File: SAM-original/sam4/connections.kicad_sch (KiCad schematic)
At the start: 23 parts, among them J18 XT60PW-M, J19 XT60PW-M, J20 XT30PW-F, J21 Conn_02x16_Odd_Even, J22 10103594-0001LF, J23 Conn_01x06_Socket, J24 Conn_01x04_Socket, J25 Conn_01x04_Socket, J26 Conn_01x04_Socket, J27 Conn_01x04_Socket, J28 Conn_01x04_Socket, J5 Conn_01x09_Socket, J6 Conn_01x02_Socket, J7 Conn_01x06_Socket, J8 Conn_01x02_Socket, SW1 SW_SPST

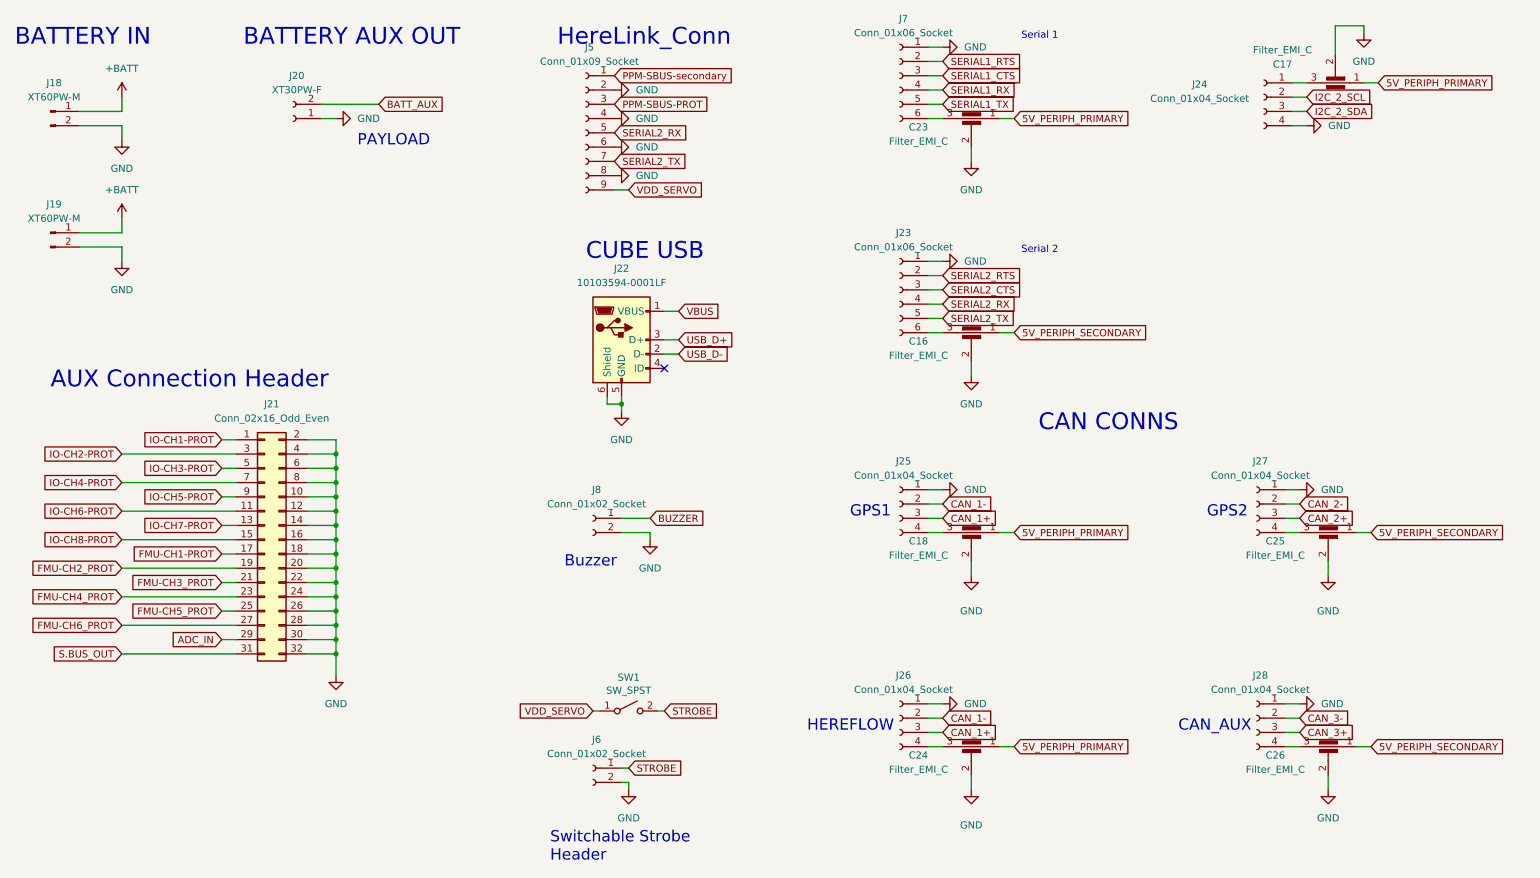
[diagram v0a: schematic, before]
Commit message: reannotate sam schem to bring into parity
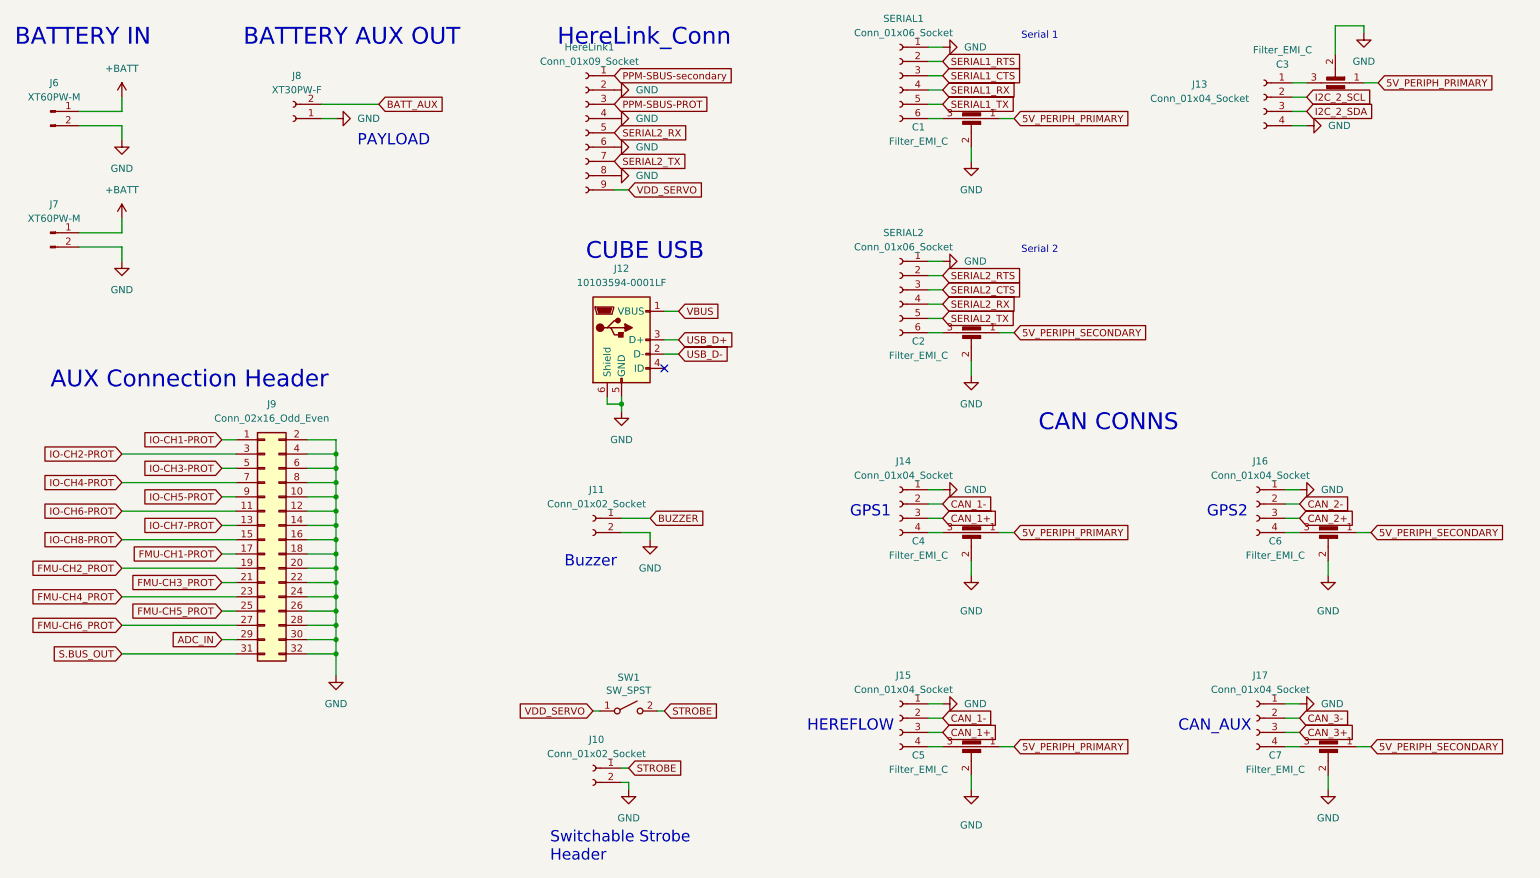
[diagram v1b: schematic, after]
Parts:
- renumbered C23 to C1, C16 to C2, C17 to C3, C18 to C4, C24 to C5, C25 to C6, C26 to C7, J5 to HereLink1, J6 to J10, J8 to J11, J22 to J12, J24 to J13, J25 to J14, J26 to J15, J27 to J16, J28 to J17, J18 to J6, J19 to J7, J20 to J8, J21 to J9, J7 to SERIAL1, J23 to SERIAL2
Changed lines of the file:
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@@
 		(on_board yes)
 		(dnp no)
-		(property "Reference" "J27"
+		(property "Reference" "J16"
 			(at 240.665 97.79 0)
 			(effects
@@
 			(project "sam4"
 				(path "/01aa8038-f16d-42dc-9377-7a3d64116781/41046e68-fc27-4dba-9c60-40afc3564538"
-					(reference "J27")
+					(reference "J16")
 					(unit 1)
 				)
@@
 		(on_board yes)
 		(dnp no)
-		(property "Reference" "J24"
+		(property "Reference" "J13"
 			(at 229.87 30.734 0)
 			(effects
@@
 			(project ""
 				(path "/01aa8038-f16d-42dc-9377-7a3d64116781/41046e68-fc27-4dba-9c60-40afc3564538"
-					(reference "J24")
+					(reference "J13")
 					(unit 1)
 				)
@@
 		(on_board yes)
 		(dnp no)
-		(property "Reference" "C24"
+		(property "Reference" "C5"
 			(at 179.832 150.114 0)
 			(effects
@@
 			(project "sam4"
 				(path "/01aa8038-f16d-42dc-9377-7a3d64116781/41046e68-fc27-4dba-9c60-40afc3564538"
-					(reference "C24")
+					(reference "C5")
 					(unit 1)
 				)
@@
 		(dnp no)
 		(fields_autoplaced yes)
-		(property "Reference" "J28"
+		(property "Reference" "J17"
 			(at 240.665 135.89 0)
 			(effects
@@
 			(project "sam4"
 				(path "/01aa8038-f16d-42dc-9377-7a3d64116781/41046e68-fc27-4dba-9c60-40afc3564538"
-					(reference "J28")
+					(reference "J17")
 					(unit 1)
 				)
@@
 		(dnp no)
 		(fields_autoplaced yes)
-		(property "Reference" "J21"
+		(property "Reference" "J9"
 			(at 64.77 87.63 0)
 			(effects
@@
 			(project ""
 				(path "/01aa8038-f16d-42dc-9377-7a3d64116781/41046e68-fc27-4dba-9c60-40afc3564538"
-					(reference "J21")
+					(reference "J9")
 					(unit 1)
 				)
@@
 		(dnp no)
 		(fields_autoplaced yes)
-		(property "Reference" "J18"
+		(property "Reference" "J6"
 			(at 26.035 30.48 0)
 			(effects
@@
 			(project ""
 				(path "/01aa8038-f16d-42dc-9377-7a3d64116781/41046e68-fc27-4dba-9c60-40afc3564538"
-					(reference "J18")
+					(reference "J6")
 					(unit 1)
 				)
@@
 		(on_board yes)
 		(dnp no)
-		(property "Reference" "C17"
+		(property "Reference" "C3"
 			(at 244.602 27.178 0)
 			(effects
@@
 			(project "sam4"
 				(path "/01aa8038-f16d-42dc-9377-7a3d64116781/41046e68-fc27-4dba-9c60-40afc3564538"
-					(reference "C17")
+					(reference "C3")
 					(unit 1)
 				)
@@
 		(on_board yes)
 		(dnp no)
-		(property "Reference" "C23"
+		(property "Reference" "C1"
 			(at 179.832 38.354 0)
 			(effects
@@
 			(project ""
 				(path "/01aa8038-f16d-42dc-9377-7a3d64116781/41046e68-fc27-4dba-9c60-40afc3564538"
-					(reference "C23")
+					(reference "C1")
 					(unit 1)
 				)
@@
 		(dnp no)
 		(fields_autoplaced yes)
-		(property "Reference" "J7"
+		(property "Reference" "SERIAL1"
 			(at 177.165 19.05 0)
 			(effects
@@
 			(project ""
 				(path "/01aa8038-f16d-42dc-9377-7a3d64116781/41046e68-fc27-4dba-9c60-40afc3564538"
-					(reference "J7")
+					(reference "SERIAL1")
 					(unit 1)
 				)
@@
 		(on_board yes)
 		(dnp no)
-		(property "Reference" "C26"
+		(property "Reference" "C7"
 			(at 243.332 150.114 0)
 			(effects
@@
 			(project "sam4"
 				(path "/01aa8038-f16d-42dc-9377-7a3d64116781/41046e68-fc27-4dba-9c60-40afc3564538"
-					(reference "C26")
+					(reference "C7")
 					(unit 1)
 				)
@@
 		(dnp no)
 		(fields_autoplaced yes)
-		(property "Reference" "J5"
+		(property "Reference" "HereLink1"
 			(at 121.285 24.13 0)
 			(effects
@@
 			(project ""
 				(path "/01aa8038-f16d-42dc-9377-7a3d64116781/41046e68-fc27-4dba-9c60-40afc3564538"
-					(reference "J5")
+					(reference "HereLink1")
 					(unit 1)
 				)
@@
 		(dnp no)
 		(fields_autoplaced yes)
-		(property "Reference" "J6"
+		(property "Reference" "J10"
 			(at 122.555 147.32 0)
 			(effects
@@
 			(project "sam4"
 				(path "/01aa8038-f16d-42dc-9377-7a3d64116781/41046e68-fc27-4dba-9c60-40afc3564538"
-					(reference "J6")
+					(reference "J10")
 					(unit 1)
 				)
@@
 		(dnp no)
 		(fields_autoplaced yes)
-		(property "Reference" "J22"
+		(property "Reference" "J12"
 			(at 127 63.5 0)
 			(effects
@@
 			(project ""
 				(path "/01aa8038-f16d-42dc-9377-7a3d64116781/41046e68-fc27-4dba-9c60-40afc3564538"
-					(reference "J22")
+					(reference "J12")
 					(unit 1)
 				)
@@
 		(dnp no)
 		(fields_autoplaced yes)
-		(property "Reference" "J8"
+		(property "Reference" "J11"
 			(at 122.555 102.87 0)
 			(effects
@@
 			(project ""
 				(path "/01aa8038-f16d-42dc-9377-7a3d64116781/41046e68-fc27-4dba-9c60-40afc3564538"
-					(reference "J8")
+					(reference "J11")
 					(unit 1)
 				)
@@
 		(dnp no)
 		(fields_autoplaced yes)
-		(property "Reference" "J19"
+		(property "Reference" "J7"
 			(at 26.035 52.07 0)
 			(effects
@@
 			(project "sam4"
 				(path "/01aa8038-f16d-42dc-9377-7a3d64116781/41046e68-fc27-4dba-9c60-40afc3564538"
-					(reference "J19")
+					(reference "J7")
 					(unit 1)
 				)
@@
 		(dnp no)
 		(fields_autoplaced yes)
-		(property "Reference" "J25"
+		(property "Reference" "J14"
 			(at 177.165 97.79 0)
 			(effects
@@
 			(project "sam4"
 				(path "/01aa8038-f16d-42dc-9377-7a3d64116781/41046e68-fc27-4dba-9c60-40afc3564538"
-					(reference "J25")
+					(reference "J14")
 					(unit 1)
 				)
@@
 		(on_board yes)
 		(dnp no)
-		(property "Reference" "C25"
+		(property "Reference" "C6"
 			(at 243.332 112.014 0)
 			(effects
@@
 			(project "sam4"
 				(path "/01aa8038-f16d-42dc-9377-7a3d64116781/41046e68-fc27-4dba-9c60-40afc3564538"
-					(reference "C25")
+					(reference "C6")
 					(unit 1)
 				)
@@
 		(dnp no)
 		(fields_autoplaced yes)
-		(property "Reference" "J23"
+		(property "Reference" "SERIAL2"
 			(at 177.165 57.15 0)
 			(effects
@@
 			(project "sam4"
 				(path "/01aa8038-f16d-42dc-9377-7a3d64116781/41046e68-fc27-4dba-9c60-40afc3564538"
-					(reference "J23")
+					(reference "SERIAL2")
 					(unit 1)
 				)
@@
 		(on_board yes)
 		(dnp no)
-		(property "Reference" "C16"
+		(property "Reference" "C2"
 			(at 179.832 76.454 0)
 			(effects
@@
 			(project "sam4"
 				(path "/01aa8038-f16d-42dc-9377-7a3d64116781/41046e68-fc27-4dba-9c60-40afc3564538"
-					(reference "C16")
+					(reference "C2")
 					(unit 1)
 				)
@@
 		(on_board yes)
 		(dnp no)
-		(property "Reference" "C18"
+		(property "Reference" "C4"
 			(at 179.832 112.014 0)
 			(effects
@@
 			(project "sam4"
 				(path "/01aa8038-f16d-42dc-9377-7a3d64116781/41046e68-fc27-4dba-9c60-40afc3564538"
-					(reference "C18")
+					(reference "C4")
 					(unit 1)
 				)
@@
 		(dnp no)
 		(fields_autoplaced yes)
-		(property "Reference" "J26"
+		(property "Reference" "J15"
 			(at 177.165 135.89 0)
 			(effects
@@
 			(project "sam4"
 				(path "/01aa8038-f16d-42dc-9377-7a3d64116781/41046e68-fc27-4dba-9c60-40afc3564538"
-					(reference "J26")
+					(reference "J15")
 					(unit 1)
 				)
@@
 		(dnp no)
 		(fields_autoplaced yes)
-		(property "Reference" "J20"
+		(property "Reference" "J8"
 			(at 69.215 29.21 0)
 			(effects
@@
 			(project ""
 				(path "/01aa8038-f16d-42dc-9377-7a3d64116781/41046e68-fc27-4dba-9c60-40afc3564538"
-					(reference "J20")
+					(reference "J8")
 					(unit 1)
 				)

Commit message: place top. revisit missing parts
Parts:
- added BUZZ1: BUZZ, aerpaw-footprints:sam_buzzer, symbol Connector:Conn_01x02_Pin
- J11: footprint (none) -> aerpaw-footprints:sam_buzzer_conn
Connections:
- net BATT_AUX: now also J8.1 (Pin_1); no longer J8.2 (Pin_2)
- net BUZZER: now also J11.2 (Pin_2); no longer J11.1 (Pin_1)
- net CAN_1+: now also J14.2 (Pin_2), J15.2 (Pin_2); no longer J14.3 (Pin_3), J15.3 (Pin_3)
- net CAN_1-: now also J14.3 (Pin_3), J15.3 (Pin_3); no longer J14.2 (Pin_2), J15.2 (Pin_2)
- net CAN_2+: now also J16.2 (Pin_2); no longer J16.3 (Pin_3)
- net CAN_2-: now also J16.3 (Pin_3); no longer J16.2 (Pin_2)
- net CAN_3+: now also J17.2 (Pin_2); no longer J17.3 (Pin_3)
- net CAN_3-: now also J17.3 (Pin_3); no longer J17.2 (Pin_2)
- net GND: now also J10.1 (Pin_1), J11.1 (Pin_1), J13.1 (Pin_1), J14.4 (Pin_4), J15.4 (Pin_4), J16.4 (Pin_4), J17.4 (Pin_4), J8.2 (Pin_2), SERIAL1.6 (Pin_6), SERIAL2.6 (Pin_6); no longer J10.2 (Pin_2), J11.2 (Pin_2), J13.4 (Pin_4), J14.1 (Pin_1), J15.1 (Pin_1), J16.1 (Pin_1), J17.1 (Pin_1), J8.1 (Pin_1), SERIAL1.1 (Pin_1), SERIAL2.1 (Pin_1)
- net I2C_2_SCL: now also J13.3 (Pin_3); no longer J13.2 (Pin_2)
- net I2C_2_SDA: now also J13.2 (Pin_2); no longer J13.3 (Pin_3)
- net SERIAL1_CTS: now also SERIAL1.4 (Pin_4); no longer SERIAL1.3 (Pin_3)
- net SERIAL1_RTS: now also SERIAL1.5 (Pin_5); no longer SERIAL1.2 (Pin_2)
- net SERIAL1_RX: now also SERIAL1.3 (Pin_3); no longer SERIAL1.4 (Pin_4)
- net SERIAL1_TX: now also SERIAL1.2 (Pin_2); no longer SERIAL1.5 (Pin_5)
- net SERIAL2_CTS: now also SERIAL2.4 (Pin_4); no longer SERIAL2.3 (Pin_3)
- net SERIAL2_RTS: now also SERIAL2.5 (Pin_5); no longer SERIAL2.2 (Pin_2)
- net SERIAL2_RX: now also SERIAL2.3 (Pin_3); no longer SERIAL2.4 (Pin_4)
- net SERIAL2_TX: now also SERIAL2.2 (Pin_2); no longer SERIAL2.5 (Pin_5)
- net STROBE: now also J10.2 (Pin_2); no longer J10.1 (Pin_1)
- net at C6.3: now also J16.1 (Pin_1); no longer J16.4 (Pin_4)
- net at C3.3: now also J13.4 (Pin_4); no longer J13.1 (Pin_1)
- net at C5.3: now also J15.1 (Pin_1); no longer J15.4 (Pin_4)
- net at C7.3: now also J17.1 (Pin_1); no longer J17.4 (Pin_4)
- net at C1.3: now also SERIAL1.1 (Pin_1); no longer SERIAL1.6 (Pin_6)
- net at C4.3: now also J14.1 (Pin_1); no longer J14.4 (Pin_4)
- net at C2.3: now also SERIAL2.1 (Pin_1); no longer SERIAL2.6 (Pin_6)
- no-connect marks 1 -> 3
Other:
- moved on the sheet: J10, J11, J13, J14, J15, J16, J17, J8, SERIAL1, SERIAL2
